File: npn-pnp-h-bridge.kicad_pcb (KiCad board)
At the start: 2 copper layers, 68.8 x 57 mm, 35 parts, among them J1 S4B-PH-K-S_LF__SN_, J2 S2B-PH-K-S_LF__SN_, Q1 MBT3904DW1, Q2 MBT3904DW1, Q3 MBT3904DW1, Q4 MBT3946DW1T1, Q5 MBT3946DW1T1, Q6 MBT3946DW1T1, Q7 MBT3946DW1T1

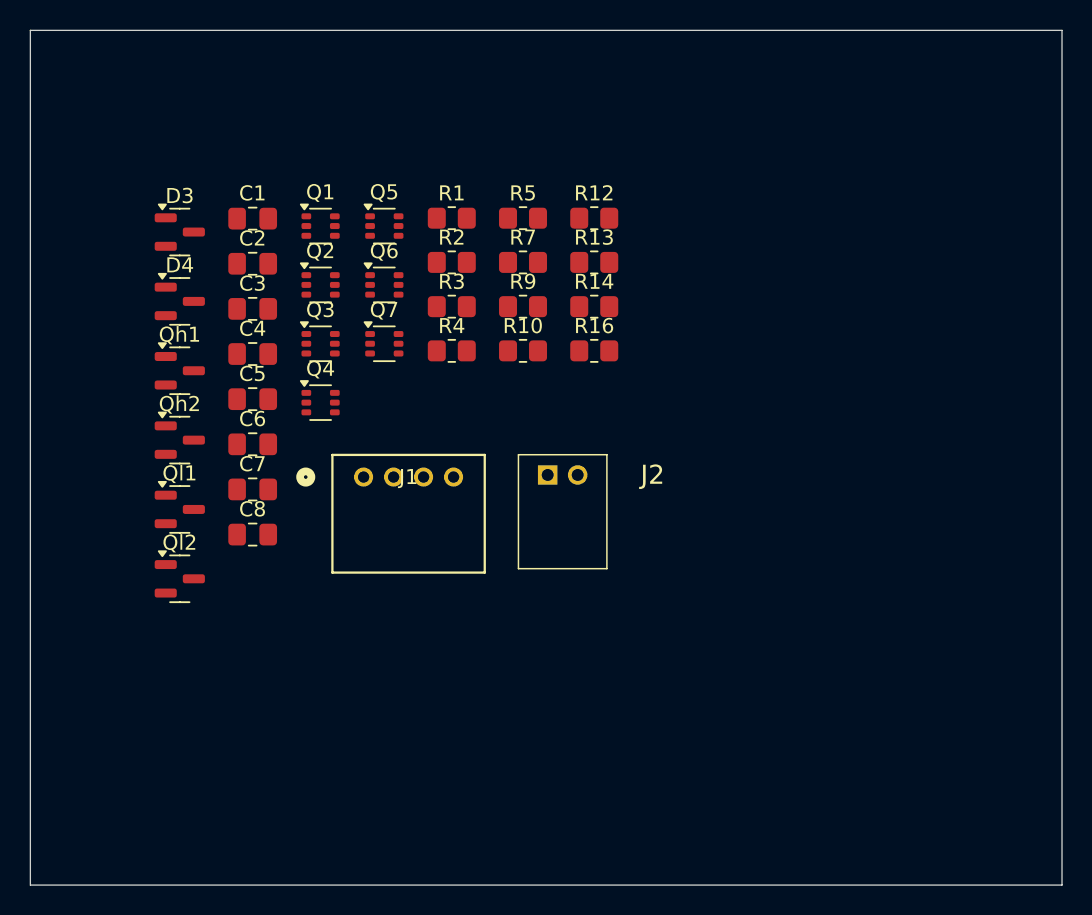
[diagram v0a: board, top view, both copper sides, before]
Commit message: fillet PCB and change transistor footprints
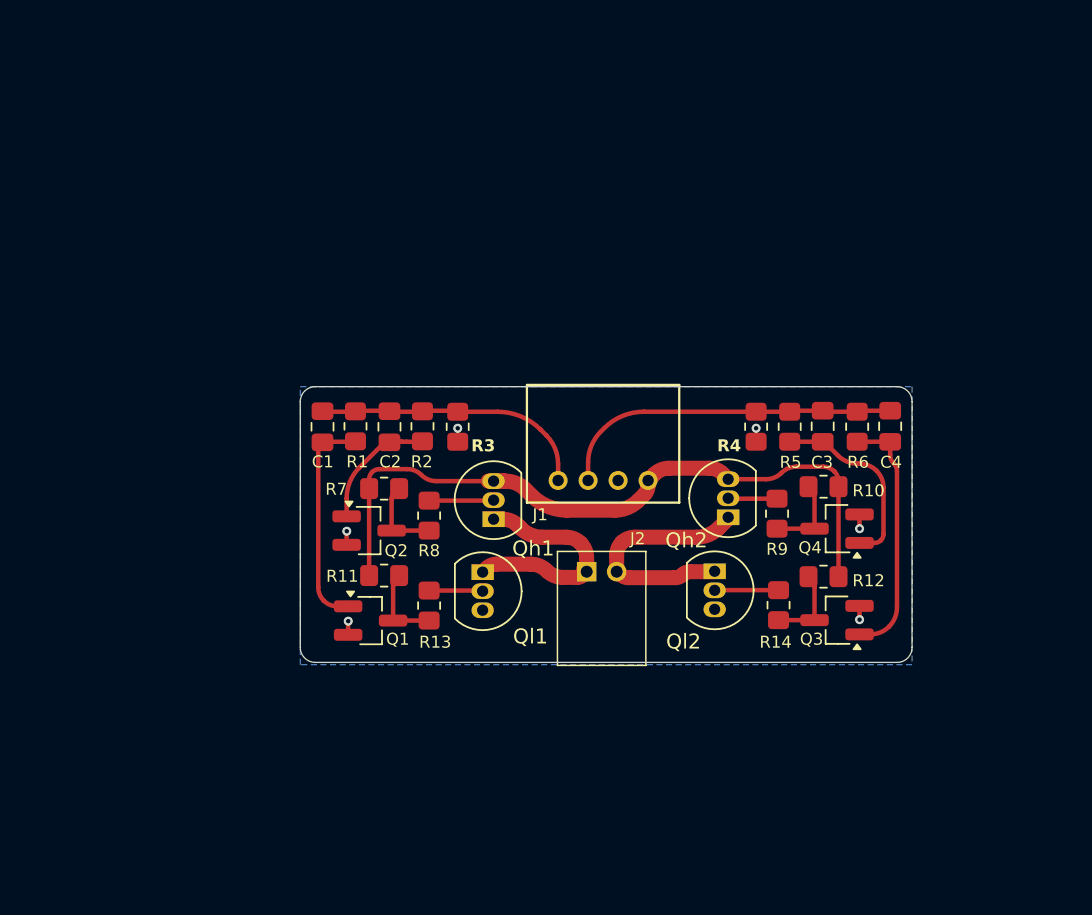
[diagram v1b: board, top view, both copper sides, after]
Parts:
- removed the C3 at (147.5, 83.7)
- removed C5, C6, C7, C8: 10p, Capacitor_SMD:C_0805_2012Metric_Pad1.18x1.45mm_HandSolder
- removed D3, D4: BAT54A, Package_TO_SOT_SMD:SOT-23
- removed Q5, Q6, Q7: MBT3946DW1T1, Package_TO_SOT_SMD:SOT-363_SC-70-6
- removed R16: 22k, Resistor_SMD:R_0805_2012Metric_Pad1.20x1.40mm_HandSolder
- removed the R5 at (165.6, 77.6)
- removed the R7 at (165.6, 80.6)
- added C1: 100p, Capacitor_SMD:C_0805_2012Metric_Pad1.18x1.45mm_HandSolder, F.Cu at (152.2, 91.5)
- added R11: 1k, Resistor_SMD:R_0805_2012Metric_Pad1.20x1.40mm_HandSolder, F.Cu at (156.3, 101.5)
- added R13: 1k, Resistor_SMD:R_0805_2012Metric_Pad1.20x1.40mm_HandSolder, F.Cu at (159.3, 103.5)
- added R14: 1k, Resistor_SMD:R_0805_2012Metric_Pad1.20x1.40mm_HandSolder, F.Cu at (182.6, 103.4)
- added R6: 2.2k, Resistor_SMD:R_0805_2012Metric_Pad1.20x1.40mm_HandSolder, F.Cu at (187.8, 91.5)
- added R8: 2k, Resistor_SMD:R_0805_2012Metric_Pad1.20x1.40mm_HandSolder, F.Cu at (159.3, 97.5)
- Q1, Q2, Q3: value MBT3904DW1 -> MMBT3904; footprint Package_TO_SOT_SMD:SOT-363_SC-70-6 -> Package_TO_SOT_SMD:SOT-23_Handsoldering
- Q4: value MBT3946DW1T1 -> MMBT3904; footprint Package_TO_SOT_SMD:SOT-363_SC-70-6 -> Package_TO_SOT_SMD:SOT-23_Handsoldering
- Qh1, Qh2: value AO3400A -> BC327; footprint Package_TO_SOT_SMD:SOT-23 -> Package_TO_SOT_THT:TO-92_Inline
- Ql1, Ql2: value AO3400A -> BC337; footprint Package_TO_SOT_SMD:SOT-23 -> Package_TO_SOT_THT:TO-92_Inline
- R1, R2: value 10 -> 2.2k
- R10: renamed from R14; value 22k -> 1k
- R12: value 22k -> 1k
- R3, R4: value 3.3k -> 220k
- R5: renamed from R13; value 3.3k -> 2.2k
- R7: renamed from R10; value 22k -> 1k
- R9: value 3.3k -> 2k
- moved C4 42.8 mm to (190.0, 91.5), turned to -90 degrees
- moved C3 39.5 mm to (185.5, 91.5), turned to -90 degrees
- moved Q3 39.1 mm to (186.5, 104.4), turned to 180 degrees
- moved Qh2 36.9 mm to (179.2, 97.6), turned to 90 degrees
- moved Ql2 35.7 mm to (178.3, 101.2), turned to -90 degrees
- moved Q4 35.5 mm to (186.5, 98.3), turned to 180 degrees
- moved R12 28.4 mm to (185.6, 101.5)
- moved Q1 26.5 mm to (155.4, 104.5)
- moved Qh1 23.2 mm to (163.6, 97.7), turned to 90 degrees
- moved R9 21.9 mm to (182.5, 97.3), turned to -90 degrees
- moved R4 20.9 mm to (181.1, 91.5), turned to 90 degrees
- moved Ql1 20.6 mm to (162.9, 101.2), turned to -90 degrees
- moved R10 19.4 mm to (185.6, 95.5)
- moved J1 19.0 mm to (173.9, 95.1), turned to 180 degrees
- moved R5 17.0 mm to (183.3, 91.5), turned to -90 degrees
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- renumbered C1 to C2, C2 to C3
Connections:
- C2 pad 2: /bQ1A -> /bQ2
- C3 pad 2: /bQ2A -> /bQ4
- C4 pad 1: /pHI -> /LO_IN
- C4 pad 2: /bQ3B -> /bQ3
- J1 pad 3: /HI_IN -> /LO_IN
- J1 pad 4: /LO_IN -> /HI_IN
- Q1 pad 1: GND -> /bQ1
- Q1 pad 2: /bQ1A -> GND
- Q1 pad 3: /HI_OUT -> Net-(Q1-C)
- Q2 pad 1: GND -> /bQ2
- Q2 pad 2: /bQ2A -> GND
- Q2 pad 3: /LO_OUT -> Net-(Q2-C)
- Q3 pad 1: GND -> /bQ3
- Q3 pad 2: /bQ3A -> GND
- Q3 pad 3: /bQ2A -> Net-(Q3-C)
- Q4 pad 1: /HI_END -> /bQ4
- Q4 pad 2: /HI_OUT -> GND
- Q4 pad 3: GND -> Net-(Q4-C)
- Qh1 pad 1: /H1g -> /O1
- Qh1 pad 2: /O1 -> /H1b
- Qh2 pad 1: /H2g -> /O2
- Qh2 pad 2: GND -> /H2b
- Qh2 pad 3: /O2 -> +5V
- Ql1 pad 1: /L1g -> /O1
- Ql1 pad 2: GND -> /L1b
- Ql1 pad 3: /O1 -> GND
- Ql2 pad 1: /L2g -> /O2
- Ql2 pad 2: /O2 -> /L2b
- Ql2 pad 3: +5V -> GND
- R1 pad 1: /HI_END -> /HI_IN
- R1 pad 2: /H1g -> /bQ1
- R10 pad 1: /bQ2B -> Net-(Q4-C)
- R12 pad 1: /HI_OUT -> Net-(Q3-C)
- R2 pad 1: /HI_END -> /HI_IN
- R2 pad 2: /H2g -> /bQ2
- R3 pad 1: /pHI -> GND
- R3 pad 2: /bQ3B -> /HI_IN
- R4 pad 1: /pLO -> GND
- R4 pad 2: /bQ3A -> /LO_IN
- R5 pad 2: /bQ2A -> /bQ4
- R7 pad 1: /bQ1B -> Net-(Q2-C)
- R9 pad 1: /HI_IN -> /H2b
- R9 pad 2: /bQ1A -> Net-(Q4-C)
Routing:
- net +5V: track 0.00 -> 48.2 mm
- net /LO_IN: track 0.00 -> 23.2 mm
- net /HI_IN: track 0.00 -> 19.2 mm
- net /bQ3: track 0.00 -> 16.9 mm
- net /O2: track 0.00 -> 16.5 mm
- net /O1: track 0.00 -> 15.8 mm
- net /bQ1: track 0.00 -> 14.7 mm
- net /bQ4: track 0.00 -> 12.7 mm
- net /bQ2: track 0.00 -> 8.37 mm
- net Net-(Q1-C): track 0.00 -> 5.53 mm
- net Net-(Q2-C): track 0.00 -> 5.53 mm
- net GND: track 0.00 -> 5.50 mm, vias 0 -> 6
- net Net-(Q4-C): track 0.00 -> 5.49 mm
- net Net-(Q3-C): track 0.00 -> 5.43 mm
- net /H1b: track 0.00 -> 4.31 mm
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- added copper zone on B.Cu, net GND
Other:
- board size 68.8 x 57 mm -> 40.8 x 18.4 mm
- board text added: "+5V"
- board text added: "GND"
- board text added: "H-Bridge for Fairylights"
- board text added: "HI_in"
- board text added: "LO_in"

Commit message: colorful nets
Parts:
- moved Qh2 0.44 mm to (178.9, 97.9)
- moved Ql2 0.34 mm to (178.3, 101.5)
- moved Qh1 0.20 mm to (163.6, 97.9)
- moved Ql1 0.20 mm to (162.9, 101.4)
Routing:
- net /O2: track 16.5 -> 10.6 mm
- net /O1: track 15.8 -> 10.3 mm

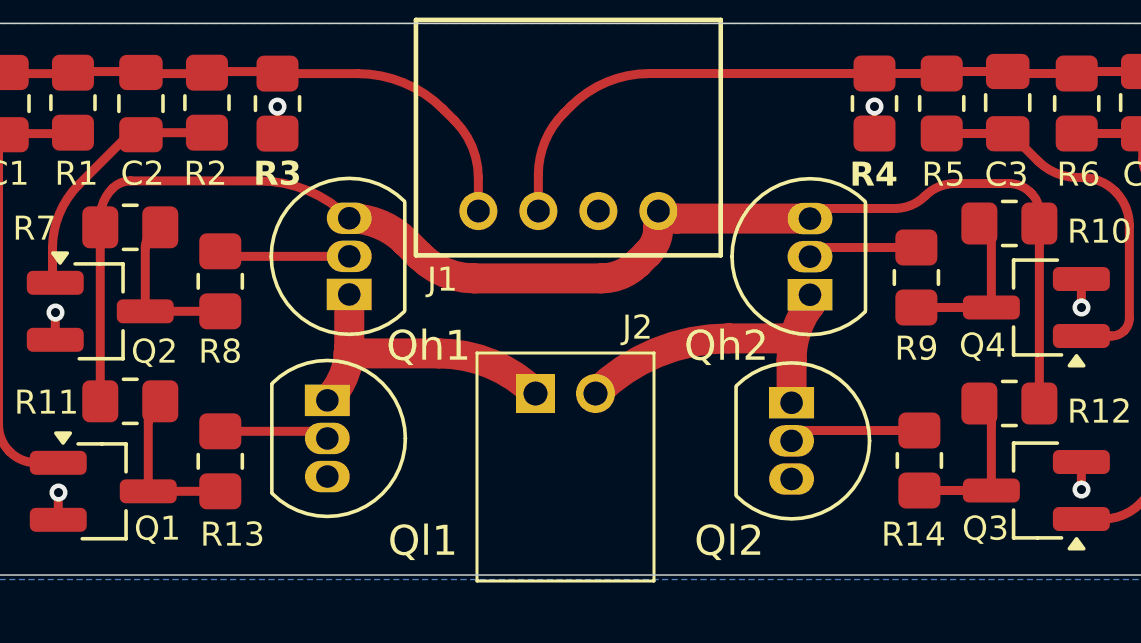
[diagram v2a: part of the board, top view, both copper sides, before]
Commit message: add optional freewheel diodes on the back layer
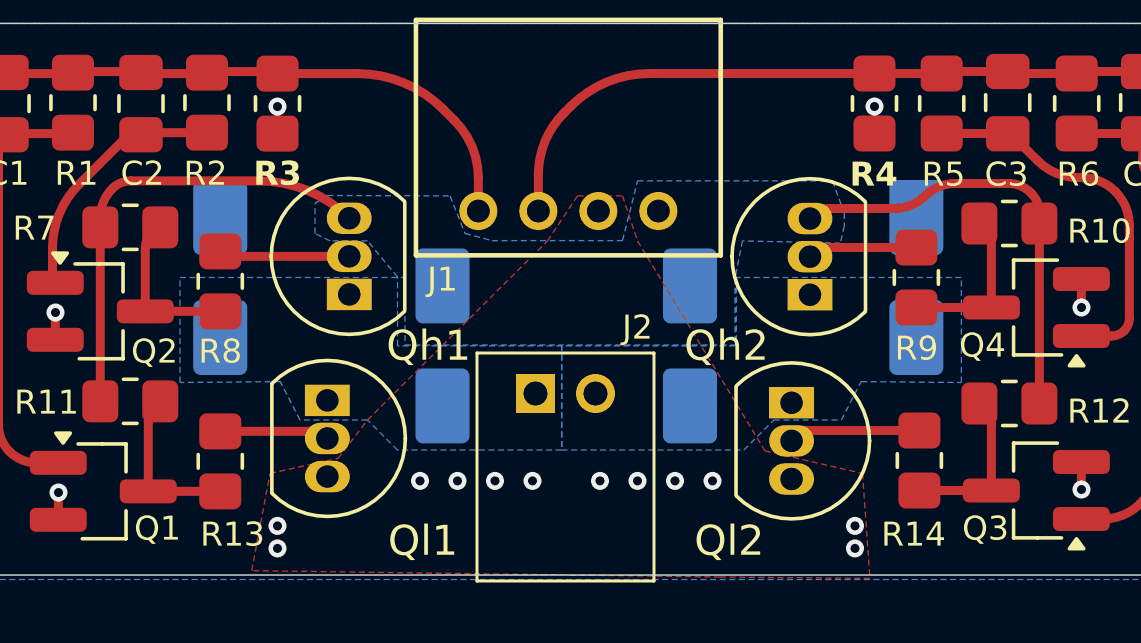
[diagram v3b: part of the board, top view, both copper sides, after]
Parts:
- added D2: SS14, Diode_SMD:D_SMA, B.Cu at (166.7, 99.6)
- added D3: SS14, Diode_SMD:D_SMA, B.Cu at (174.9, 99.6)
- added D4: SS14, Diode_SMD:D_SMA, B.Cu at (159.3, 97.3)
- added D5: SS14, Diode_SMD:D_SMA, B.Cu at (182.5, 97.3)
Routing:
- net +5V: track 47.8 -> 30.4 mm
- net /O2: track 10.6 -> 0.00 mm
- net /O1: track 10.3 -> 0.00 mm
- net GND: vias 6 -> 18
- added copper zone on B.Cu, net +5V
- added copper zone on B.Cu, net /O1
- added copper zone on B.Cu, net /O2
- added copper zone on F.Cu, net GND

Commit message: Thanks PCBWay for sponsoring prototypes of the new revision\!
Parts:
- renumbered D2 to D1, D4 to D2, D5 to D4, Qh1 to Ql1, Ql1 to Ql2, Qh2 to Qr1, Ql2 to Qr2
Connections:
- net /HI_IN renamed /L_IN
- net /LO_IN renamed /R_IN
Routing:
- net GND: vias 18 -> 14
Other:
- board text added: "L_in"
- board text added: "R_in"
- board text removed: "HI_in"
- board text removed: "LO_in"

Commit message: update bom
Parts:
- R1, R2, R5, R6: value 2.2k -> 680
- R10, R7: value 1k -> 10k
- R13, R14: value 1k -> 100
- R8, R9: value 2k -> 180
